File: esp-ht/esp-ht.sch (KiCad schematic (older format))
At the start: 25 parts, among them P1 CONN_01X02, P2 CONN_01X02, SW1 SW_PUSH_SMALL, SW2 SW_PUSH_SMALL, U1 ESP-12E, U2 MCP1700-3.0, U3 SI7021

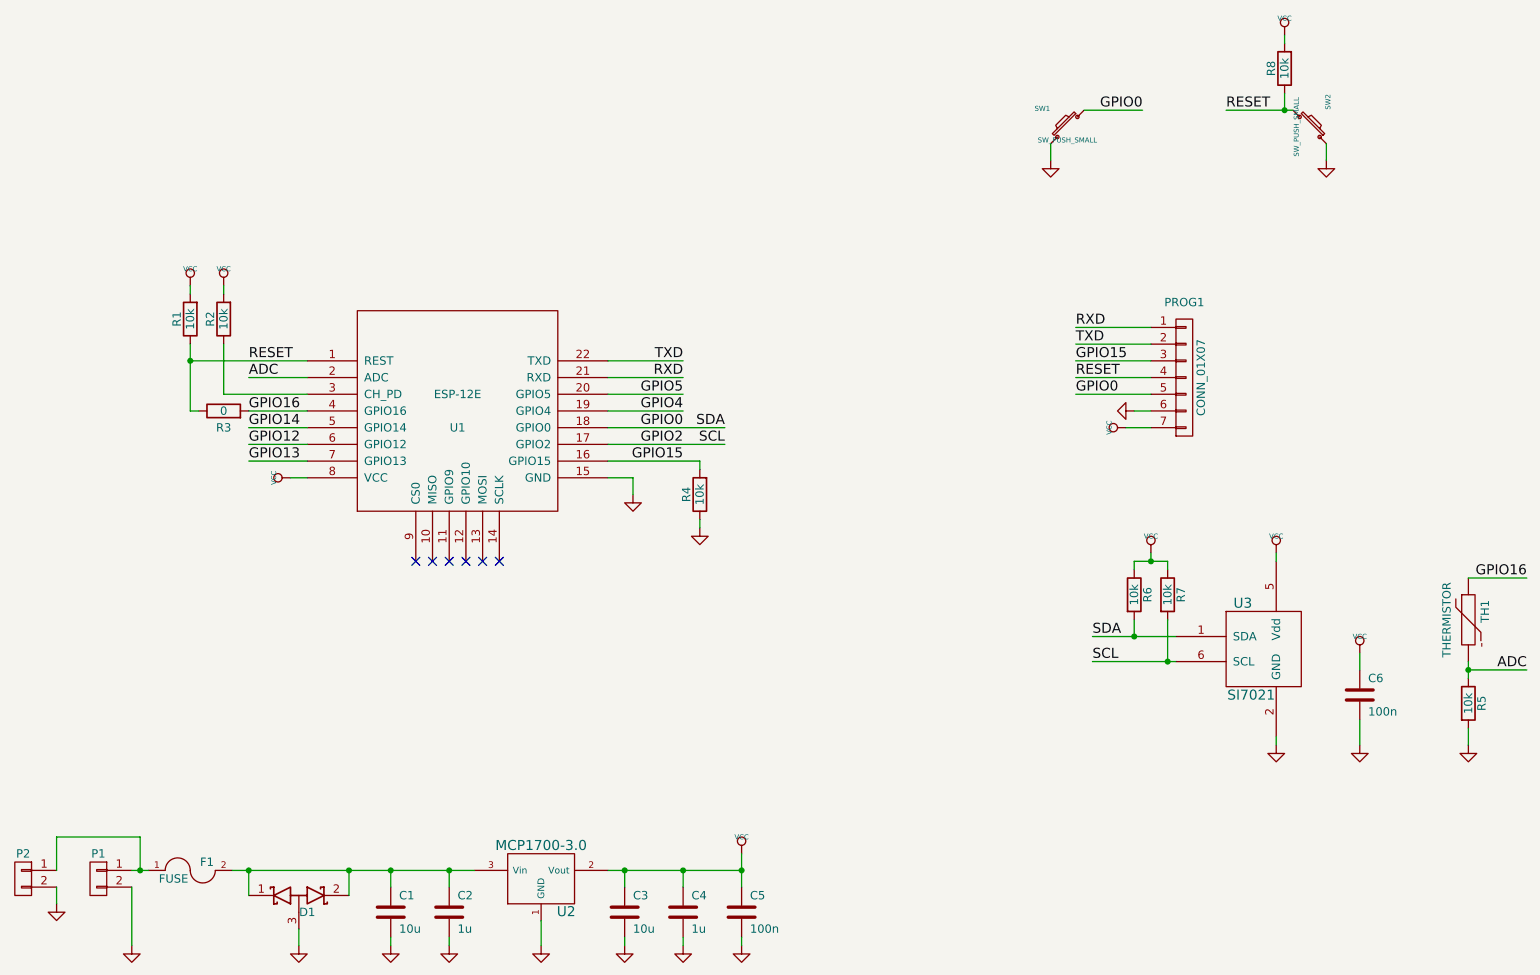
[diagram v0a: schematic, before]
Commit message: BMP180 pressure sensor added to the circuit
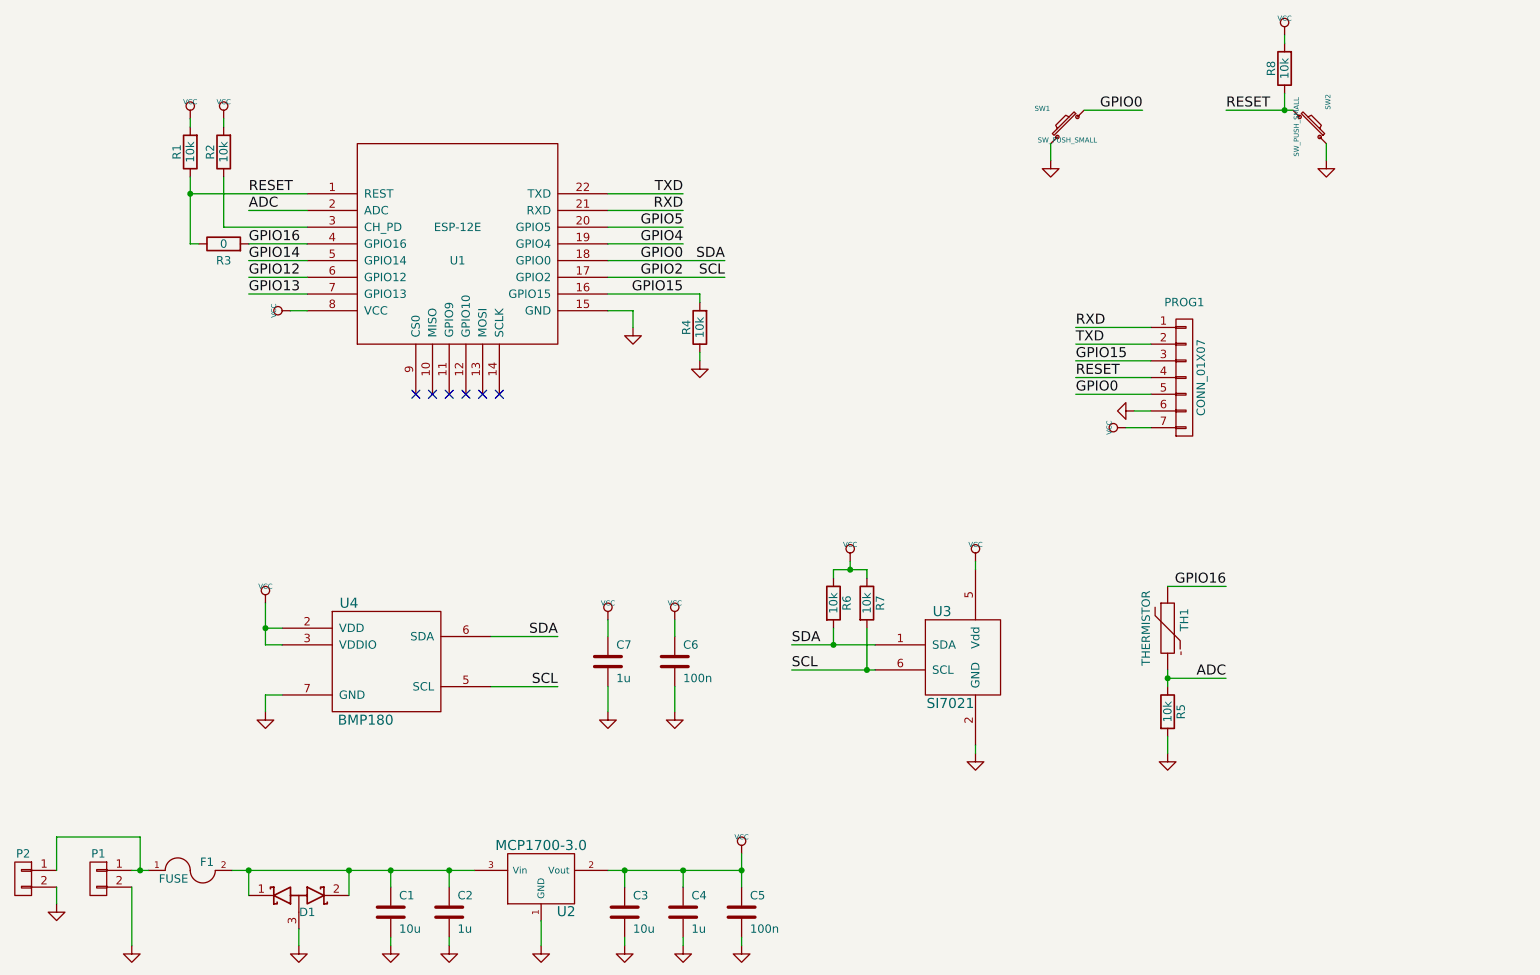
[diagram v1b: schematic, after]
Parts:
- added C7: 1u, mysmd:SM0603S, symbol C
- added U4: BMP180, mysmd:BMP180, symbol BMP180
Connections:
- net GND: now also C7.2, U4.7 (GND)
- net GPIO0: now also U4.6 (SDA)
- net GPIO2: now also U4.5 (SCL)
- net VCC: now also C7.1, U4.2 (VDD), U4.3 (VDDIO)
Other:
- moved on the sheet: C6, R1, R2, R3, R4, R5, R6, R7, TH1, U1, U3

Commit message: repeated Pull-up resistor (R1)  to RESET removed
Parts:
- removed R1: 10k, mysmd:SM0603S, symbol R

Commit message: Version changed
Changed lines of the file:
@@
 LIBS:microchip-mcp125x-xxx
 LIBS:toshiba
+LIBS:ESP8266
 LIBS:esp-ht-cache
 EELAYER 25 0
@@
 encoding utf-8
 Sheet 1 1
-Title "panStamp Humidity and Temperature board for ESP8266"
+Title "panStamp ambient sensor board for ESP8266"
 Date "2015-11-28"
 Rev "1.0"
@@
 	2700 4850 2600 4850
 Wire Wire Line
-	2600 4950 2600 4700
+	2600 4950 2600 4850
+Wire Wire Line
+	2600 4850 2600 4700
 Wire Wire Line
 	2700 4950 2600 4950
@@
 	8000 5150 8350 5150
 Wire Wire Line
-	8000 5200 8000 5100
+	8000 5200 8000 5150
+Wire Wire Line
+	8000 5150 8000 5100
 Wire Wire Line
 	8000 5500 8000 5600
@@
 	7900 3450 7450 3450
 Wire Wire Line
-	1900 6300 1800 6300
+	1900 6300 1850 6300
+Wire Wire Line
+	1850 6300 1800 6300
 Wire Wire Line
 	3350 6400 3350 6300
@@
 	3350 6750 3350 6700
 Wire Wire Line
-	5450 6200 5450 6400
-Wire Wire Line
-	4650 6300 5450 6300
+	5450 6200 5450 6300
+Wire Wire Line
+	5450 6300 5450 6400
+Wire Wire Line
+	4650 6300 4750 6300
+Wire Wire Line
+	4750 6300 5100 6300
+Wire Wire Line
+	5100 6300 5450 6300
 Wire Wire Line
 	4250 6750 4250 6600
@@
 	3700 6300 3700 6400
 Wire Wire Line
-	2400 6300 3850 6300
+	2400 6300 2500 6300
+Wire Wire Line
+	2500 6300 3100 6300
+Wire Wire Line
+	3100 6300 3350 6300
+Wire Wire Line
+	3350 6300 3700 6300
+Wire Wire Line
+	3700 6300 3850 6300
 Wire Wire Line
 	3700 6750 3700 6700
@@
 	8700 1650 8700 1750
 Wire Wire Line
-	8750 1750 8350 1750
+	8750 1750 8700 1750
+Wire Wire Line
+	8700 1750 8350 1750
 Wire Wire Line
 	2150 2250 2850 2250
@@
 	6200 4500 6200 4550
 Wire Wire Line
-	6000 4500 6200 4500
+	6000 4500 6100 4500
+Wire Wire Line
+	6100 4500 6200 4500
 Wire Wire Line
 	6000 4550 6000 4500
@@
 	6850 5600 6850 5550
 Wire Wire Line
-	5750 5100 6250 5100
-Wire Wire Line
-	5750 4950 6250 4950
+	5750 5100 6200 5100
+Wire Wire Line
+	6200 5100 6250 5100
+Wire Wire Line
+	5750 4950 6000 4950
+Wire Wire Line
+	6000 4950 6250 4950
 Wire Wire Line
 	6850 4500 6850 4450
